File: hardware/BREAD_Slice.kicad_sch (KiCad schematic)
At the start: 0 parts

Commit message: Finished draft 1, still need documentation and review
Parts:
- added D3: MM3Z18VT1G, Diode_SMD:D_SOD-323, symbol Device:D
- added J2: Screw_Terminal_01x06, TerminalBlock_Phoenix:TerminalBlock_Phoenix_PT-1,5-6-3.5-H_1x06_P3.50mm_Horizontal, symbol Connector:Screw_Terminal_01x06
- added J3: Screw_Terminal_01x02, TerminalBlock_Phoenix:TerminalBlock_Phoenix_PT-1,5-2-3.5-H_1x02_P3.50mm_Horizontal, symbol Connector:Screw_Terminal_01x02
- added J4: Screw_Terminal_01x08, TerminalBlock_Phoenix:TerminalBlock_Phoenix_PT-1,5-8-3.5-H_1x08_P3.50mm_Horizontal, symbol Connector:Screw_Terminal_01x08
- added R1, R10, R11, R12, R2, R3, R4, R5, R6, R7, R8, R9: 1k, Resistor_SMD:R_0603_1608Metric, symbol Device:R
- added R13, R14, R15, R19: 2.4k, Resistor_SMD:R_0603_1608Metric, symbol Device:R
- added R16, R17, R18, R20: 47, Resistor_SMD:R_0603_1608Metric, symbol Device:R
- added R21: 100k, Resistor_SMD:R_0603_1608Metric, symbol Device:R
- added SW3: SW_SPDT, Button_Switch_THT:SW_Slide-03_Wuerth-WS-SLTV_10x2.5x6.4_P2.54mm, symbol Switch:SW_SPDT
- added U10, U11, U8, U9: CPC1002N, Package_SO:SOP-4_3.8x4.1mm_P2.54mm, symbol Relay_SolidState:CPC1002N
- added U12: NTGS4111PT1G, TSOP6_3P1X1P7_ONS, symbol Transistor_FET:NTGS4111PT1G
- added U2, U3, U4, U5, U6, U7: LTV-817S, Package_DIP:SMDIP-4_W9.53mm, symbol Isolator:LTV-817S
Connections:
- net +12V: now also SW3.3 (A)
- net +5V: now also U2.4, U3.4, U4.4, U5.4, U6.4, U7.4
- net GND: now also J3.2 (Pin_2), R1.2, R13.2, R14.2, R15.2, R16.2, R17.2, R18.2, R19.2, R2.2, R20.2, R21.2, R3.2, R4.2, R5.2, R6.2, U2.2, U3.2, U4.2, U5.2, U6.2, U7.2
- new net: R13.1, U8.2
- new net: R9.1, U4.1
- new net: J2.3 (Pin_3), R9.2
- new net: R16.1, U8.3
- new net: D3.2 (A), R21.1, U12.3 (GATE)
- new net: D3.1 (K), SW3.2 (C), U12.4 (SOURCE)
- new net: R8.1, U3.1
- new net: R11.1, U6.1
- new net: R14.1, U9.2
- new net: R17.1, U9.3
- new net: J2.2 (Pin_2), R8.2
- new net: R19.1, U11.2
- new net: R20.1, U11.3
- new net: R10.1, U5.1
- new net: R12.1, U7.1
- new net: R15.1, U10.2
- new net: R7.1, U2.1
- new net: J2.1 (Pin_1), R7.2
- new net: R18.1, U10.3
- new net 24V: J3.1 (Pin_1), U12.1 (DRAIN), U12.2 (DRAIN), U12.5 (DRAIN), U12.6 (DRAIN)
- new net IN1: R1.1, U2.3
- new net IN2: R2.1, U3.3
- new net IN3: R3.1, U4.3
- new net IN4: R4.1, U5.3
- new net IN4B: J2.4 (Pin_4), R10.2
- new net IN5: R5.1, U6.3
- new net IN5B: J2.5 (Pin_5), R11.2
- new net IN6: R6.1, U7.3
- new net IN6B: J2.6 (Pin_6), R12.2
- new net OUT1: U8.1
- new net OUT1B: J4.2 (Pin_2), U8.4
- new net OUT2: U9.1
- new net OUT2B: J4.4 (Pin_4), U9.4
- new net OUT3: U10.1
- new net OUT3B: J4.6 (Pin_6), U10.4
- new net OUT4: U11.1
- new net OUT4B: J4.8 (Pin_8), U11.4
- new net VOUT: J4.1 (Pin_1), J4.3 (Pin_3), J4.5 (Pin_5), J4.7 (Pin_7), SW3.1 (B)
- no-connect marks 19 -> 9

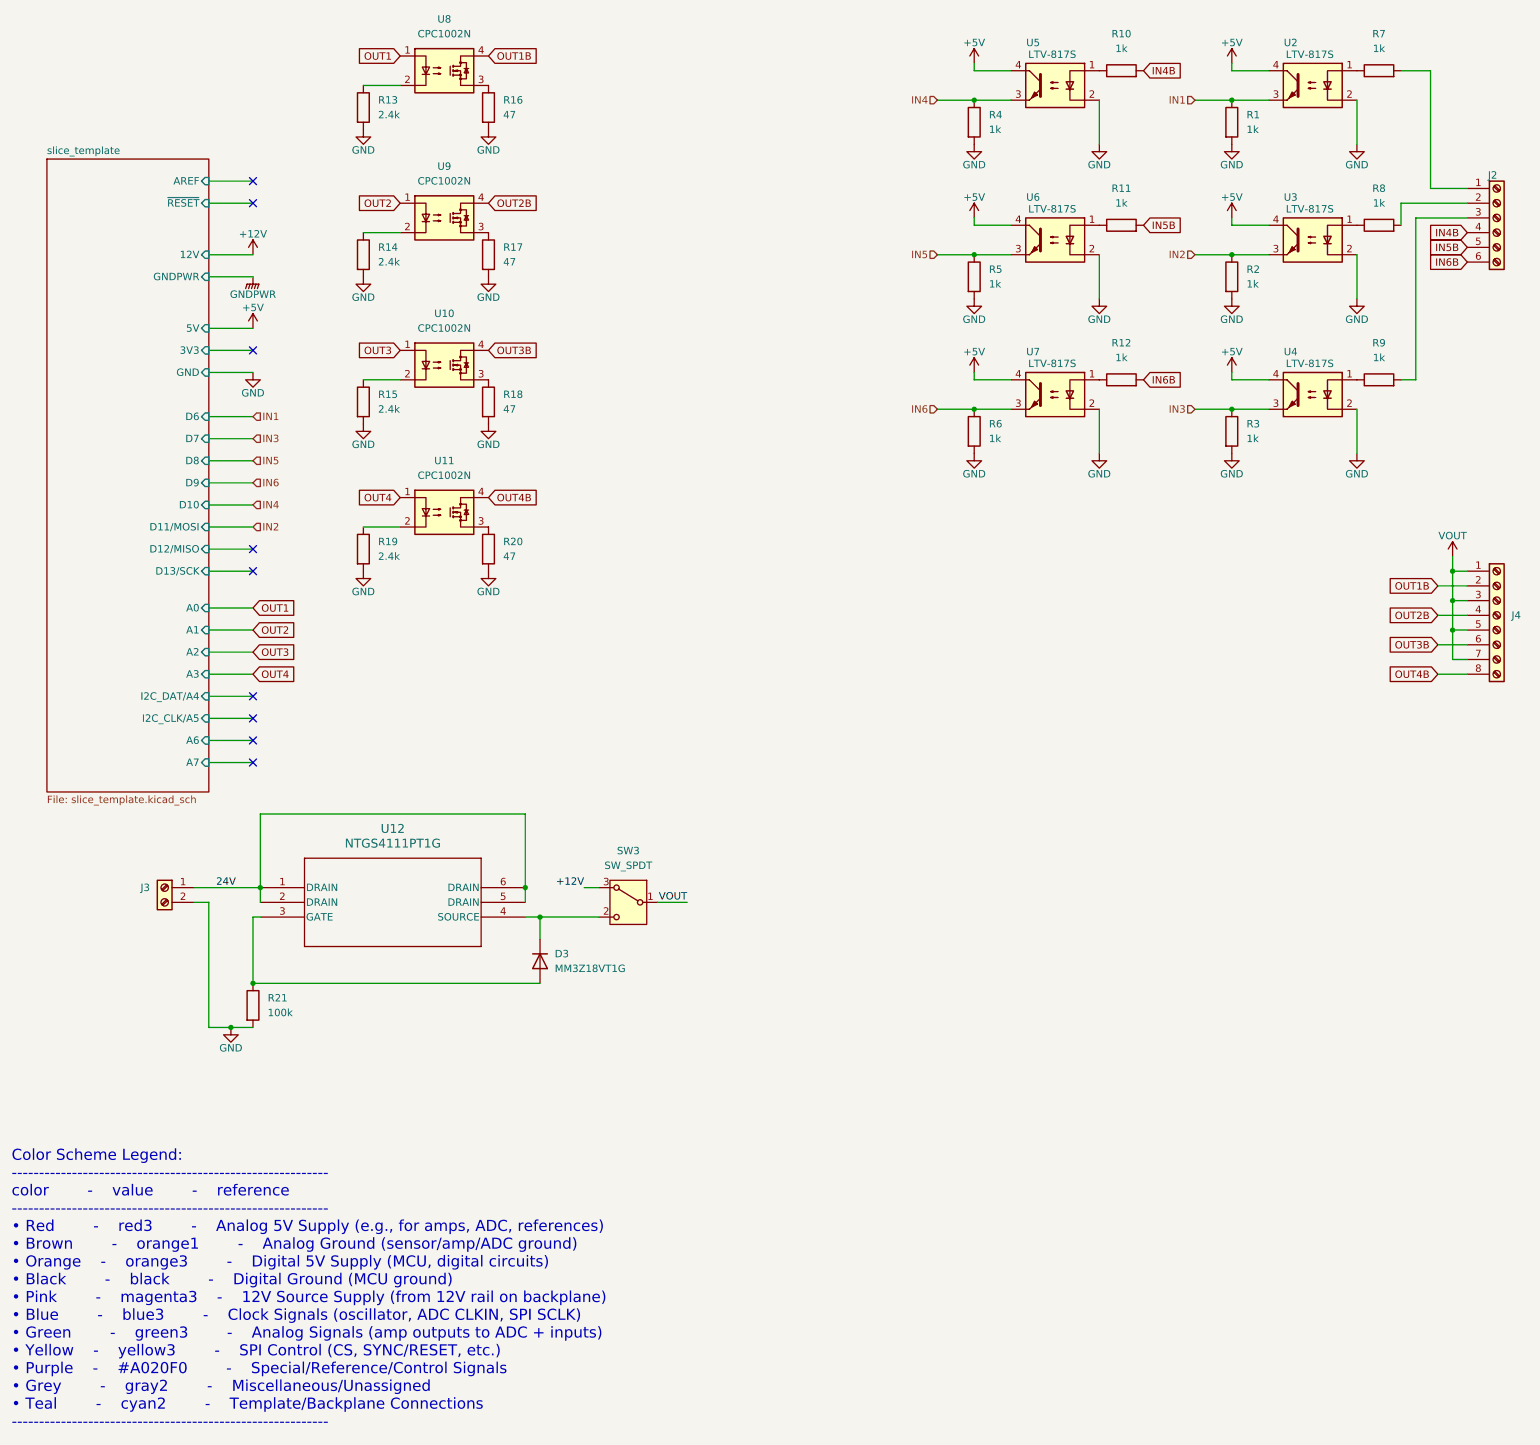
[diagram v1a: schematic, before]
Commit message: Added new conenctor
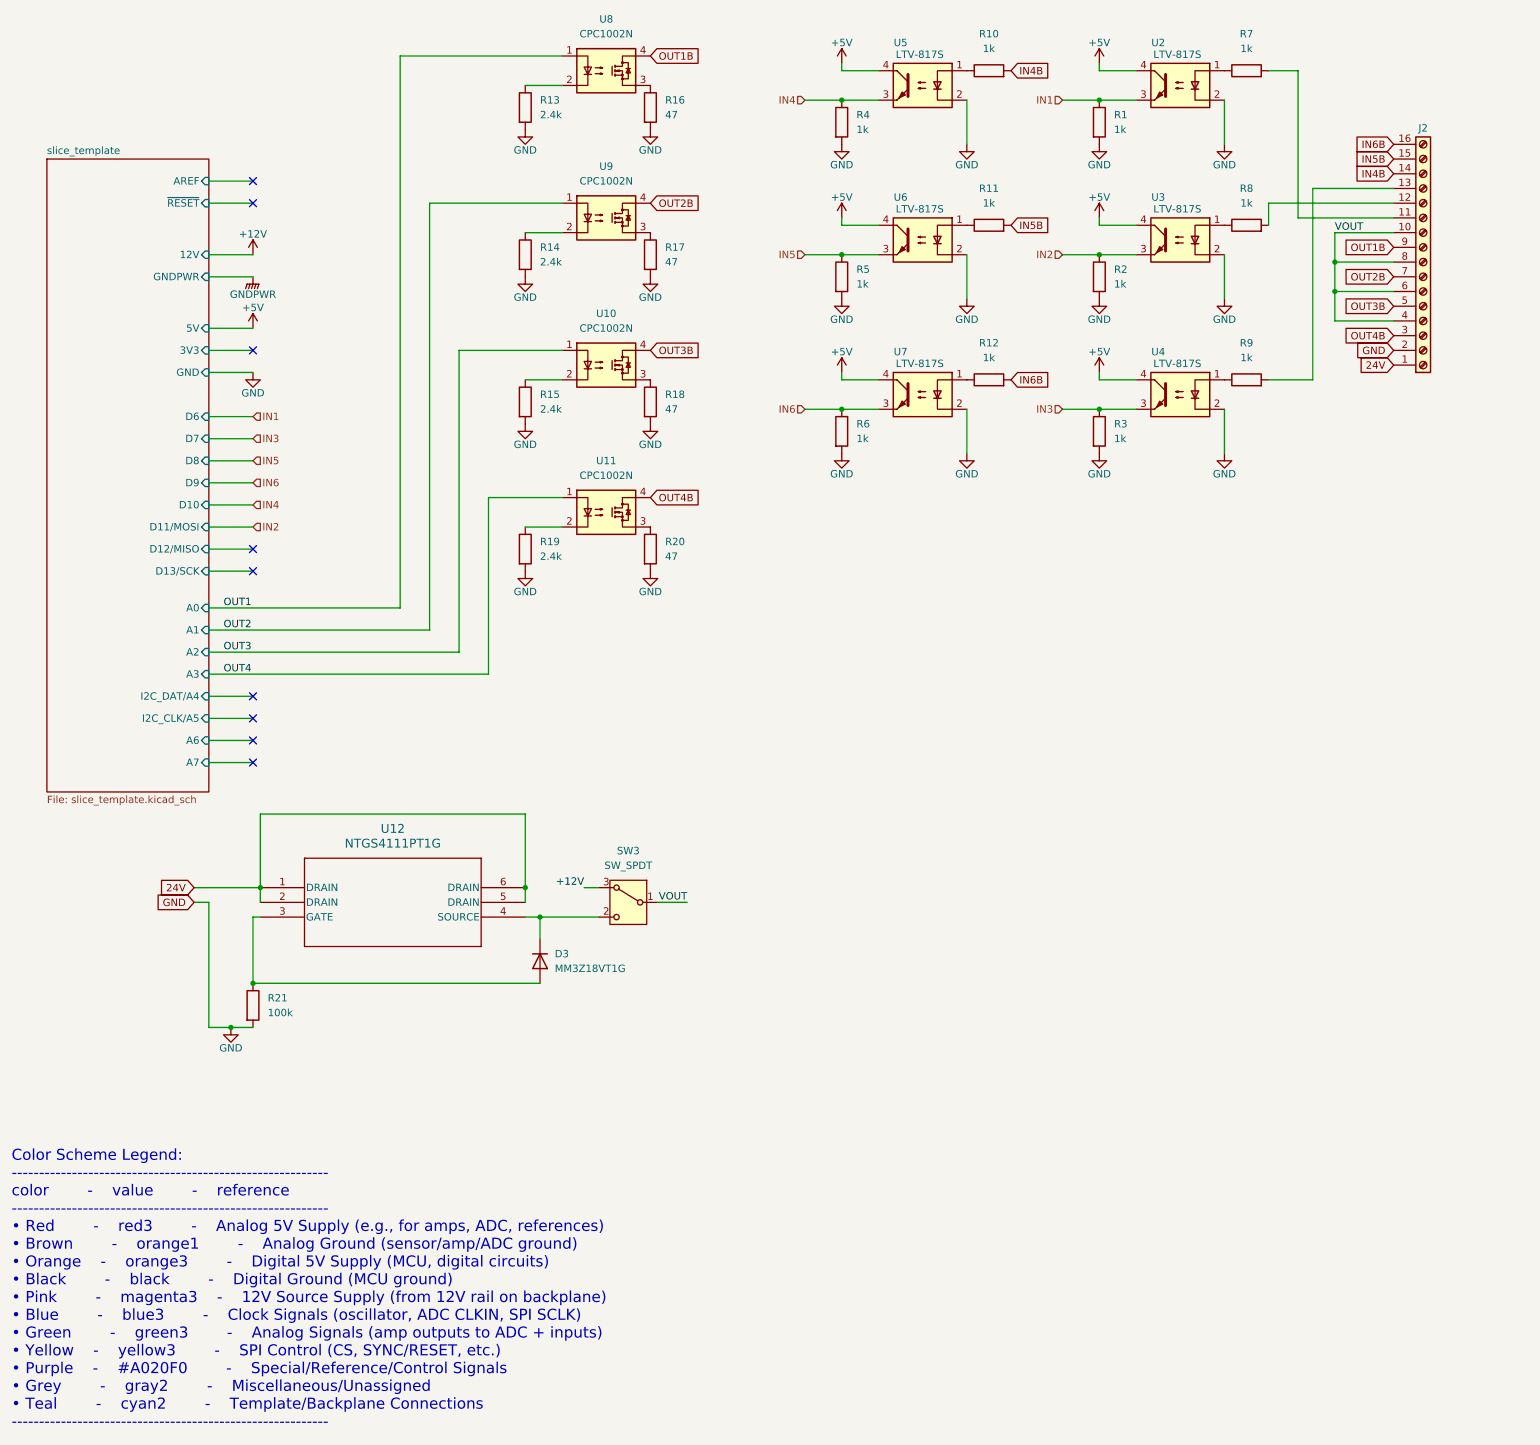
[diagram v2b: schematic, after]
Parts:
- removed J2: Screw_Terminal_01x06, TerminalBlock_Phoenix:TerminalBlock_Phoenix_PT-1,5-6-3.5-H_1x06_P3.50mm_Horizontal, symbol Connector:Screw_Terminal_01x06
- removed J3: Screw_Terminal_01x02, TerminalBlock_Phoenix:TerminalBlock_Phoenix_PT-1,5-2-3.5-H_1x02_P3.50mm_Horizontal, symbol Connector:Screw_Terminal_01x02
- removed J4: Screw_Terminal_01x08, TerminalBlock_Phoenix:TerminalBlock_Phoenix_PT-1,5-8-3.5-H_1x08_P3.50mm_Horizontal, symbol Connector:Screw_Terminal_01x08
- added J2: Screw_Terminal_01x16, kml-custom:1990148, symbol Connector:Screw_Terminal_01x16
- U12: footprint TSOP6_3P1X1P7_ONS -> Package_SO:TSOP-6_1.65x3.05mm_P0.95mm
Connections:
- net 24V: now also J2.1 (Pin_1)
- net GND: now also J2.2 (Pin_2)
- net IN4B: now also J2.14 (Pin_14)
- net IN5B: now also J2.15 (Pin_15)
- net IN6B: now also J2.16 (Pin_16)
- net OUT1B: now also J2.9 (Pin_9)
- net OUT2B: now also J2.7 (Pin_7)
- net OUT3B: now also J2.5 (Pin_5)
- net OUT4B: now also J2.3 (Pin_3)
- net VOUT: now also J2.10 (Pin_10), J2.4 (Pin_4), J2.6 (Pin_6), J2.8 (Pin_8)
- net at R9.2: now also J2.13 (Pin_13)
- net at R8.2: now also J2.12 (Pin_12)
- net at R7.2: now also J2.11 (Pin_11)
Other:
- title: (none) -> Digital IO Slice
- moved on the sheet: R1, R10, R11, R12, R13, R14, R15, R16, R17, R18, R19, R2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
